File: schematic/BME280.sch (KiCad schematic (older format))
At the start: 9 parts, among them J1 Conn_02x04_Odd_Even, U1 BME280, U2 DizzyBITLogo

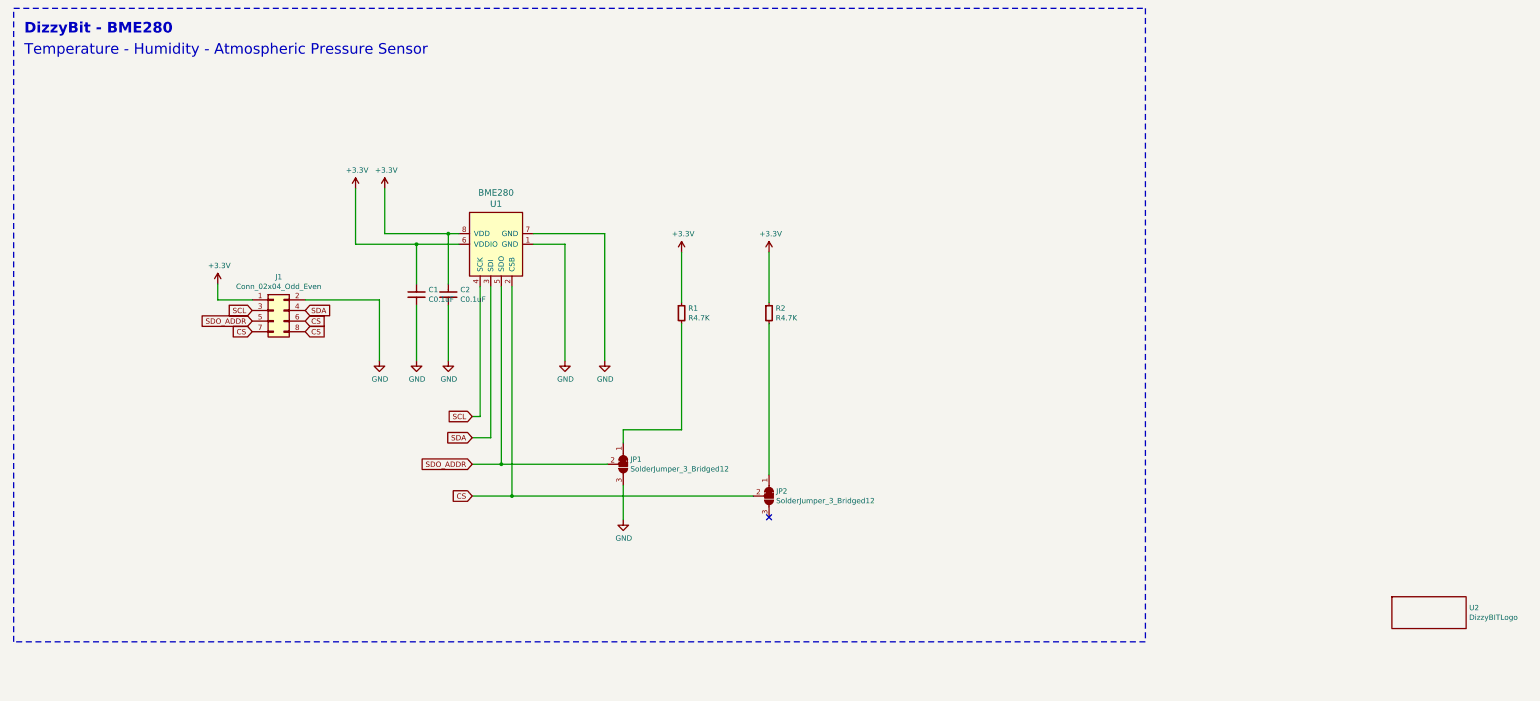
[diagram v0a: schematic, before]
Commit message: Changed pin numbers
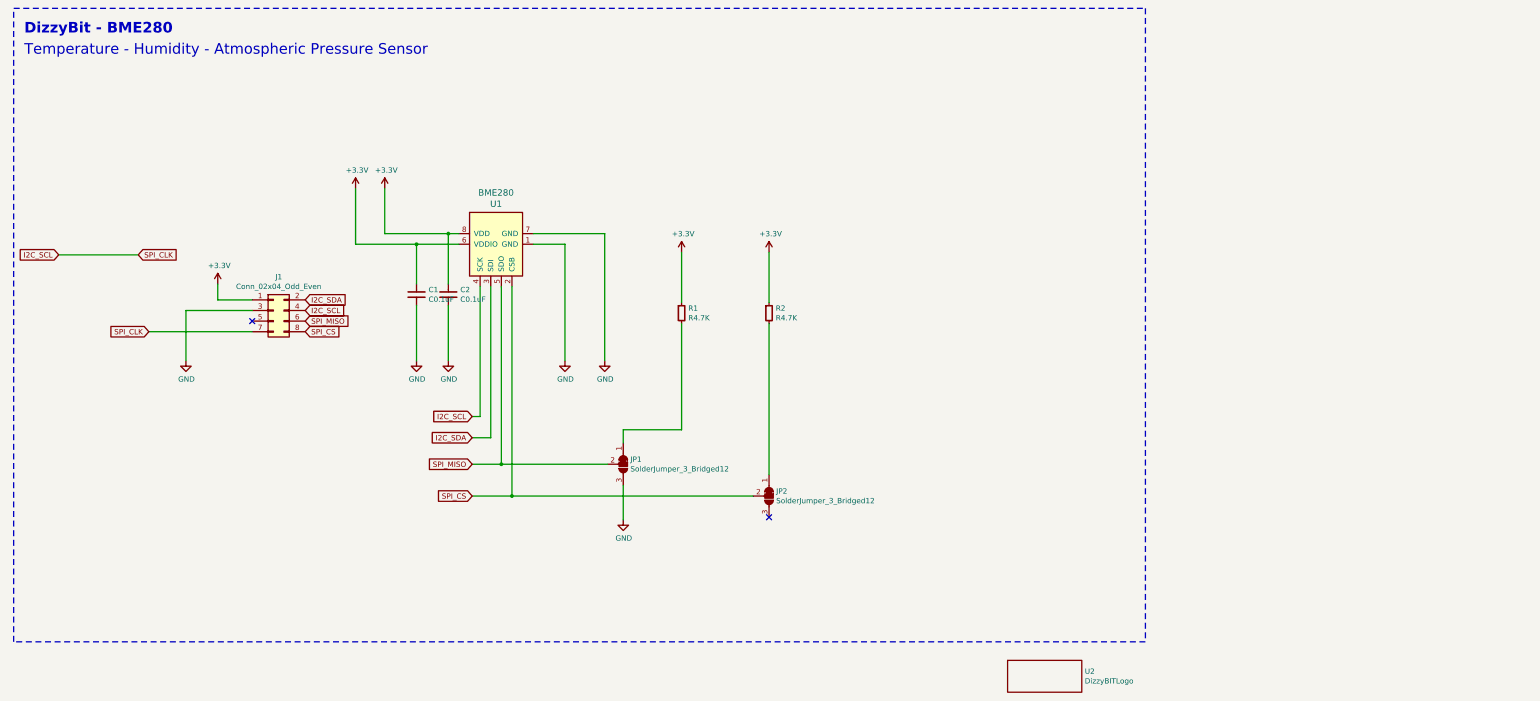
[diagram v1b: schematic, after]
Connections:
- net GND: now also J1.3 (Pin_3); no longer J1.2 (Pin_2)
- net CS renamed SPI_CS
- net SPI_CS: no longer J1.6 (Pin_6), J1.7 (Pin_7)
- net SCL renamed I2C_SCL
- net I2C_SCL: now also J1.4 (Pin_4), J1.7 (Pin_7); no longer J1.3 (Pin_3)
- net SDA renamed I2C_SDA
- net I2C_SDA: now also J1.2 (Pin_2); no longer J1.4 (Pin_4)
- net SDO_ADDR renamed SPI_MISO
- net SPI_MISO: now also J1.6 (Pin_6); no longer J1.5 (Pin_5)
- no-connect marks 1 -> 2
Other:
- moved on the sheet: U2
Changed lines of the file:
@@
 EESchema Schematic File Version 4
+LIBS:BME280-cache
 EELAYER 26 0
 EELAYER END
@@
 L undo:DizzyBITLogo U2
 U 1 1 5C903A70
-P 13875 6225
-F 0 "U2" H 14253 6271 50  0000 L CNN
-F 1 "DizzyBITLogo" H 14253 6180 50  0000 L CNN
-F 2 "undo:DizzyBIT_silk_6.4" H 13875 6225 50  0001 C CNN
-F 3 "" H 13875 6225 50  0001 C CNN
-	1    13875 6225
+P 10250 6825
+F 0 "U2" H 10628 6871 50  0000 L CNN
+F 1 "DizzyBITLogo" H 10628 6780 50  0000 L CNN
+F 2 "undo:DizzyBIT_silk_6.4" H 10250 6825 50  0001 C CNN
+F 3 "" H 10250 6825 50  0001 C CNN
+	1    10250 6825
 	1    0    0    -1
 $EndComp
@@
 L power:GND #PWR0103
 U 1 1 5C9DFFA8
-P 3975 3850
-F 0 "#PWR0103" H 3975 3600 50  0001 C CNN
-F 1 "GND" H 3980 3677 50  0000 C CNN
-F 2 "" H 3975 3850 50  0001 C CNN
-F 3 "" H 3975 3850 50  0001 C CNN
-	1    3975 3850
-	1    0    0    -1
-$EndComp
-Wire Wire Line
-	3275 3275 3975 3275
-Wire Wire Line
-	3975 3275 3975 3850
-Wire Wire Line
-	2450 3125 2450 3275
-Wire Wire Line
-	2450 3275 2775 3275
+P 2150 3850
+F 0 "#PWR0103" H 2150 3600 50  0001 C CNN
+F 1 "GND" H 2155 3677 50  0000 C CNN
+F 2 "" H 2150 3850 50  0001 C CNN
+F 3 "" H 2150 3850 50  0001 C CNN
+	1    2150 3850
+	1    0    0    -1
+$EndComp
 $Comp
 L power:+3.3V #PWR0101
@@
 	5725 2750 5725 3850
 Text GLabel 4850 4375 0    50   Input ~ 0
-SCL
+I2C_SCL
 Wire Wire Line
 	4925 3150 4925 4375
@@
 	4925 4375 4850 4375
 Text GLabel 4850 4575 0    50   Input ~ 0
-SDA
+I2C_SDA
 Wire Wire Line
 	5025 3150 5025 4575
 Wire Wire Line
 	5025 4575 4850 4575
-Text GLabel 4850 4825 0    50   Input ~ 0
-SDO_ADDR
 Wire Wire Line
 	4850 4825 5125 4825
 Wire Wire Line
 	5125 4825 5125 3150
-Text GLabel 4850 5125 0    50   Input ~ 0
-CS
 Wire Wire Line
 	4850 5125 5225 5125
@@
 	5225 5125 7500 5125
 Connection ~ 5225 5125
-Text GLabel 2775 3375 0    50   Input ~ 0
-SCL
 Text GLabel 3275 3375 2    50   Input ~ 0
-SDA
+I2C_SCL
+Text GLabel 3275 3275 2    50   Input ~ 0
+I2C_SDA
 Connection ~ 5125 4825
 $Comp
@@
 Wire Wire Line
 	6825 3300 6825 2825
-Text GLabel 2775 3475 0    50   Input ~ 0
-SDO_ADDR
-Text GLabel 2775 3575 0    50   Input ~ 0
-CS
 Text GLabel 3275 3475 2    50   Input ~ 0
-CS
-Text GLabel 3275 3575 2    50   Input ~ 0
-CS
+SPI_MISO
 $Comp
 L _passive:R R2
@@
 Text Notes 625  975  0    100  ~ 0
 Temperature - Humidity - Atmospheric‎ Pressure Sensor
+Wire Wire Line
+	2450 3125 2450 3275
+Wire Wire Line
+	2450 3275 2775 3275
+Wire Wire Line
+	2775 3375 2150 3375
+Wire Wire Line
+	2150 3375 2150 3850
+Text GLabel 3275 3575 2    50   Input ~ 0
+SPI_CS
+Text GLabel 950  2850 0    50   Input ~ 0
+I2C_SCL
+Text GLabel 4850 5125 0    50   Input ~ 0
+SPI_CS
+NoConn ~ 2775 3475
+Text GLabel 4850 4825 0    50   Input ~ 0
+SPI_MISO
+Text GLabel 1800 3575 0    50   Input ~ 0
+SPI_CLK
+Wire Wire Line
+	2775 3575 1800 3575
+Text GLabel 1700 2850 2    50   Input ~ 0
+SPI_CLK
+Wire Wire Line
+	1700 2850 950  2850
 $EndSCHEMATC
